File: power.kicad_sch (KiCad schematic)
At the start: 22 parts, among them J10 DC Barrel Jack, Q1 AO4262E, U2 TLV76733, U3 LM74700, U4 LMR33620CQ5

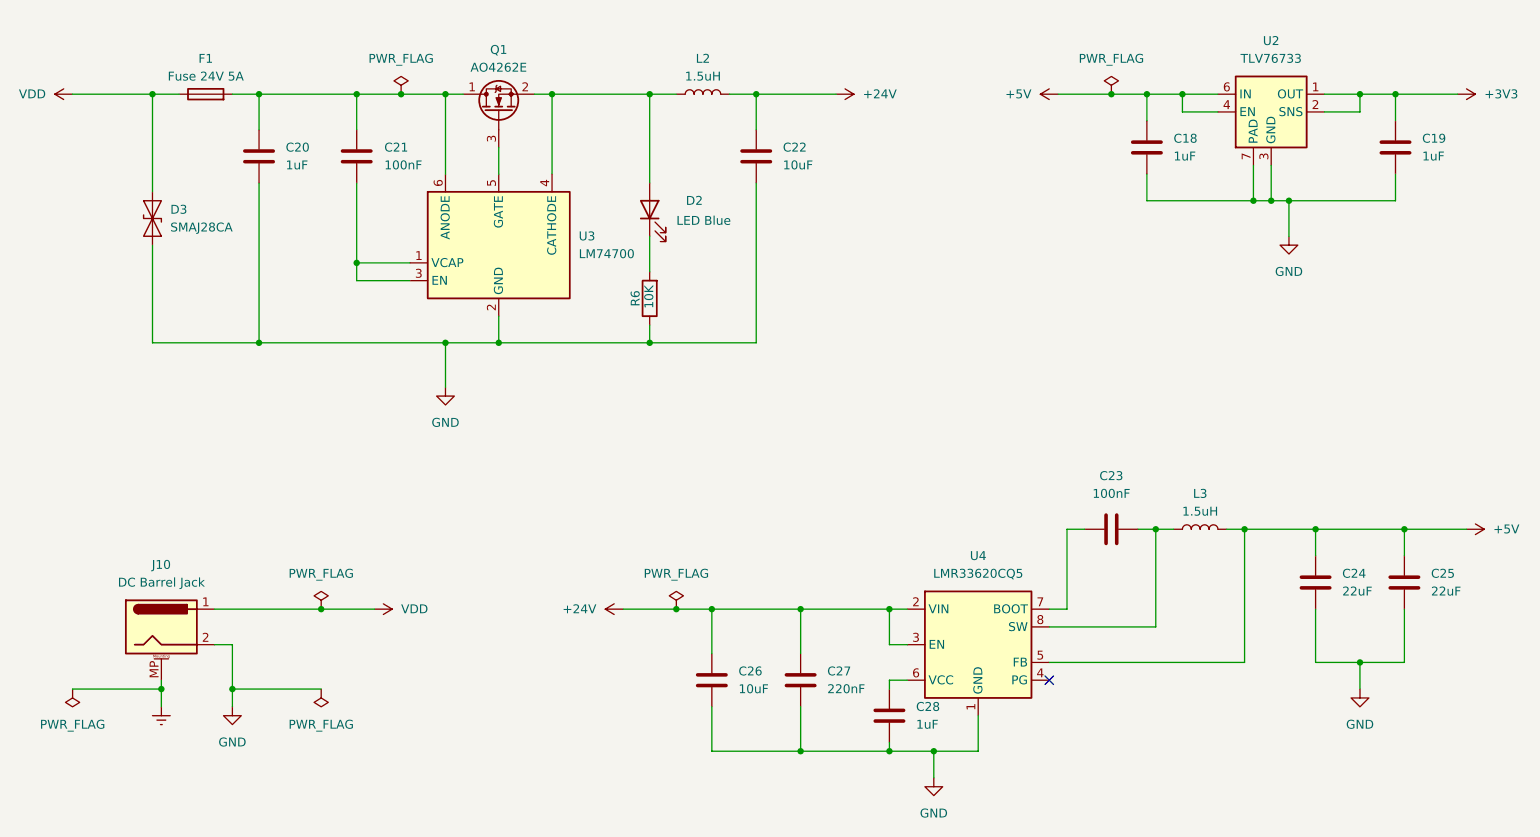
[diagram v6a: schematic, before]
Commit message: Optimized components by cost and footprint size
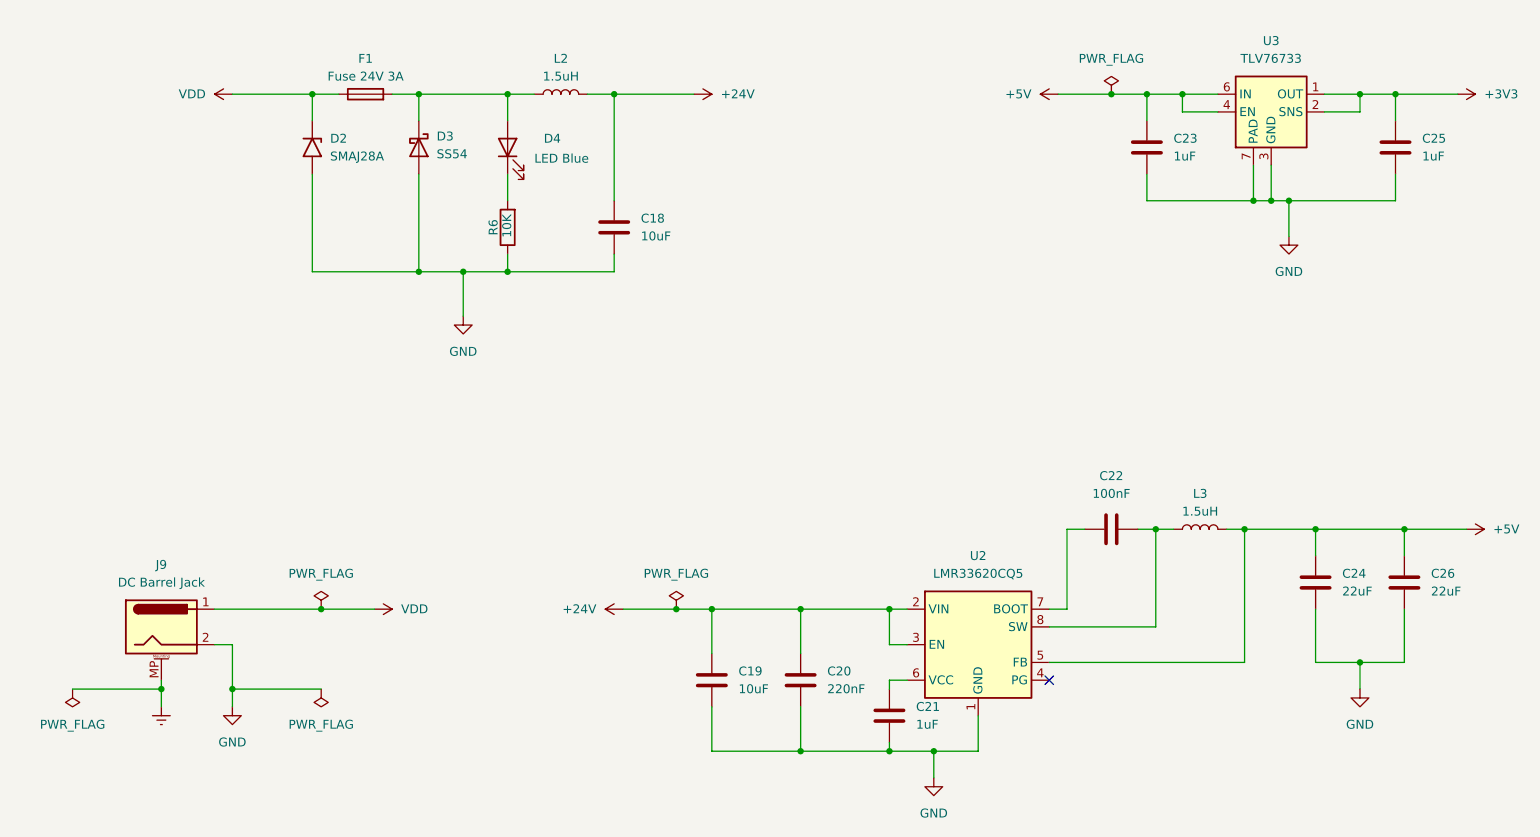
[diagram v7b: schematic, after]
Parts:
- removed C20: 1uF, Capacitor_SMD:C_0805_2012Metric_Pad1.18x1.45mm_HandSolder, symbol Device:C
- removed C21: 100nF, Capacitor_SMD:C_0603_1608Metric_Pad1.08x0.95mm_HandSolder, symbol Device:C
- removed D3: SMAJ28CA, Diode_SMD:D_SMA, symbol Diode:SMAJ28CA
- removed Q1: AO4262E, Package_SO:SOIC-8_3.9x4.9mm_P1.27mm, symbol Device:Q_NMOS_DSG
- removed U3: LM74700, Package_TO_SOT_SMD:SOT-23-6, symbol Power_Management:LM74700
- added D2: SMAJ28A, Diode_SMD:D_SMA, symbol Diode:SMAJ28A
- added D3: SS54, Diode_SMD:D_SMC, symbol Device:D_Schottky
- F1: value Fuse 24V 5A -> Fuse 24V 3A; footprint Fuse:Fuse_2920_7451Metric_Pad2.10x5.45mm_HandSolder -> Fuse:Fuse_1812_4532Metric_Pad1.30x3.40mm_HandSolder
- renumbered C22 to C18, C26 to C19, C27 to C20, C28 to C21, C23 to C22, C18 to C23, C19 to C25, C25 to C26, D2 to D4, J10 to J9, U4 to U2, U2 to U3
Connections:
- net GND: now also D2.2 (A2), D3.2 (A)
- net VDD: now also D2.1 (A1)
- net at D4.2 (A), L2.1: now also F1.2, D3.1 (K)
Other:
- moved on the sheet: C18, D4, F1, L2, R6

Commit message: Excluded rare components
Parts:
- removed C18: 10uF, Capacitor_SMD:C_1206_3216Metric_Pad1.33x1.80mm_HandSolder, symbol Device:C
- removed L2: 1.5uH, Inductor_SMD:L_Bourns_SRP5030T, symbol Device:L
- removed U2: LMR33620CQ5, Package_SO:Texas_HSOP-8-1EP_3.9x4.9mm_P1.27mm_ThermalVias, symbol Regulator_Switching:LMR33620ADDA
- added R7: 100K, Resistor_SMD:R_0603_1608Metric_Pad0.98x0.95mm_HandSolder, symbol Device:R
- added R8: 24K9, Resistor_SMD:R_0603_1608Metric_Pad0.98x0.95mm_HandSolder, symbol Device:R
- added U2: LMR33630B, Package_SO:Texas_HSOP-8-1EP_3.9x4.9mm_P1.27mm_ThermalVias, symbol Regulator_Switching:LMR33630ADDA
- L2: renamed from L3; value 1.5uH -> 2.2uH; footprint Inductor_SMD:L_Bourns_SRP5030T -> Inductor_SMD:L_10.4x10.4_H4.8
- renumbered C23 to C22, C22 to C23
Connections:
- net Earth is gone; now on net GND: J9.MP (MountPin)
- net +24V: now also D3.1 (K), D4.2 (A), F1.2, U2.2 (VIN), U2.3 (EN)
- net +5V: now also R7.2
- net GND: now also R8.1, U2.1 (GND), U2.9 (GND)
- net at C21.1: now also U2.6 (VCC)
- net at C23.1: now also U2.7 (BOOT)
- net at C23.2, L2.1: now also U2.8 (SW)
- new net: R7.1, R8.2, U2.5 (FB)
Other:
- moved on the sheet: C19, C20, C21, C22, C23, C24, C25, C26, D2, D3, D4, F1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
